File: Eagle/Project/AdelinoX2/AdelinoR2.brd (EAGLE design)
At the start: 47 x 53.3 mm, 80 parts, among them J1 DC-044-A, J2 YELLOW-8P-2.54, J3 YELLOW-6P-2.54, J4 YELLOW-8P-2.54, J5 YELLOW-8P-2.54, J6 4P-2.0, J7 YELLOW-2X3P-2.54, J8 4P-2.0, Q1 NCE3407A, Q2 CJ2305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

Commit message: Preparing pcb for Revision A.
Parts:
- D1: value SMBJ15CA-13-F -> TVS-DIODE-SZOPL-SMBJ15CA-13-F
- moved C21 0.25 mm to (15.6, 36.2)
- moved C20 0.19 mm to (42.8, 36.1)
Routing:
- net GND: track 93.3 -> 78.1 mm, vias 74 -> 136
- net PIN_D0: track 130.6 -> 129.4 mm, vias 4 -> 5
- net +3V3: track 110.2 -> 111.5 mm, vias 15 -> 22
- net PIN_A0: track 36.6 -> 35.5 mm
- net AT_SS: track 65.8 -> 65.3 mm
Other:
- board text added: "7-15V"
- board text added: "Adelino X2 http://adelino.cc Product Validation Designed in Brazil"
- board text added: "DC IN"
- board text added: "Grove I2C"
- board text added: "Grove UART"
- board text added: "HW 1.0.0 Rev A 16-01-2019"
- board text added: "MISO"
- board text added: "MOSI"
- board text added: "RX"
- board text added: "SCK"
- board text added: "SCL"
- board text added: "SDA"
- board text added: "TX"
- board text added: "VCC"
- board text removed: "Adelino X2 http://neoautus.com Product Validation Designed in Brazil"
- board text removed: "RX/TX"
- board text removed: "SCL/SDA"

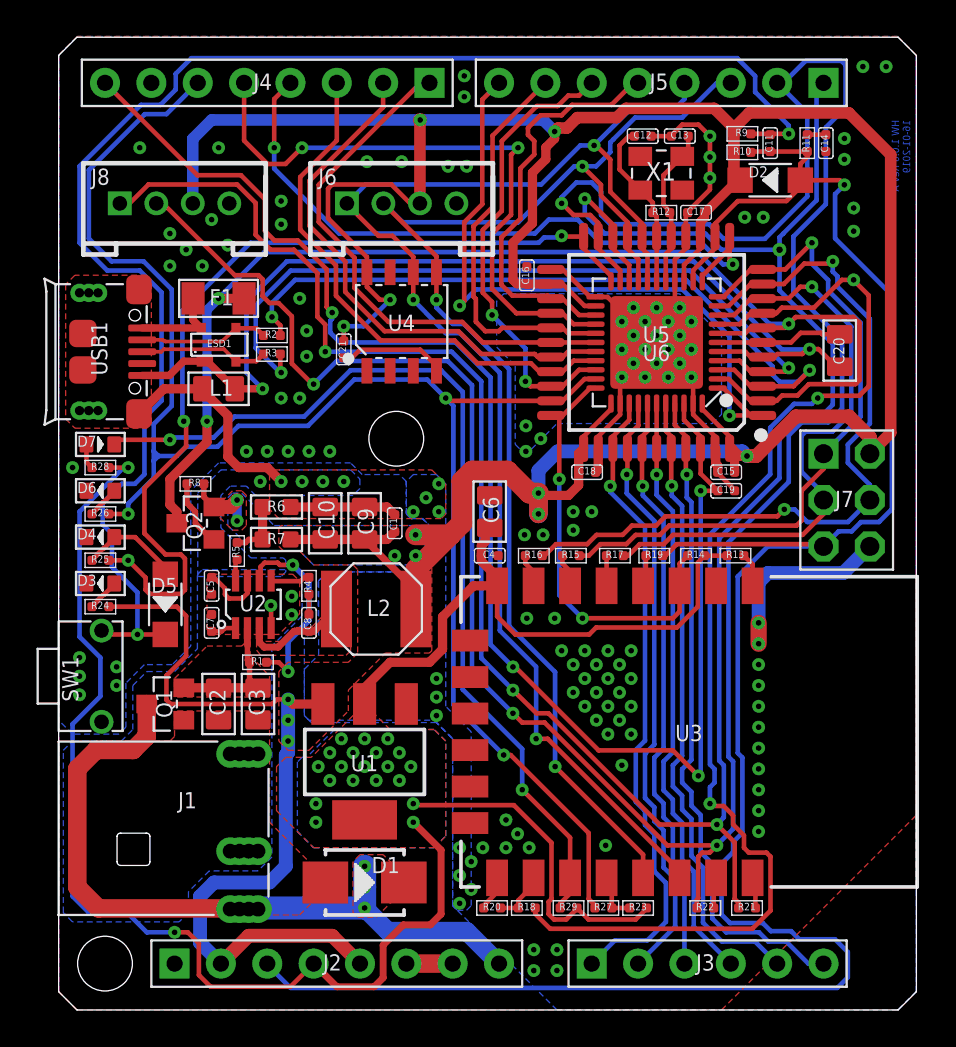
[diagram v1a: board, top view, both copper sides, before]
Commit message: Better ground plane polygon, avoiding swps areas.
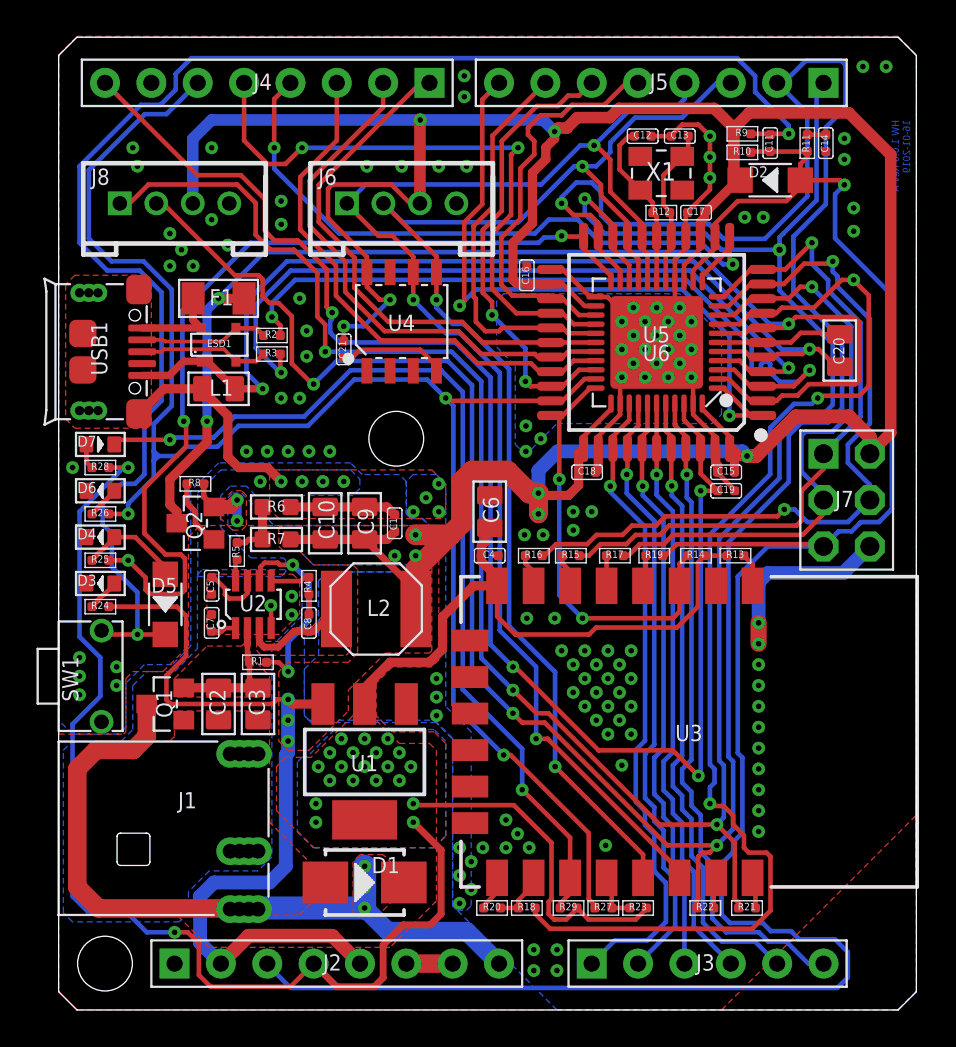
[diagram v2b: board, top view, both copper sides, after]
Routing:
- net GND: track 78.1 -> 76.5 mm, vias 136 -> 137
- net D-: track 40.6 -> 41.8 mm
